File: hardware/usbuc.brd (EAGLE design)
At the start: 24.1 x 20.3 mm, 15 parts, among them J1 PROGRAM, J2 DEVICE, U1 NCP551, U2 AT25SF081-XMHD-T, U3 PIC32MX250F128B-I_ML, Y1 8MHz

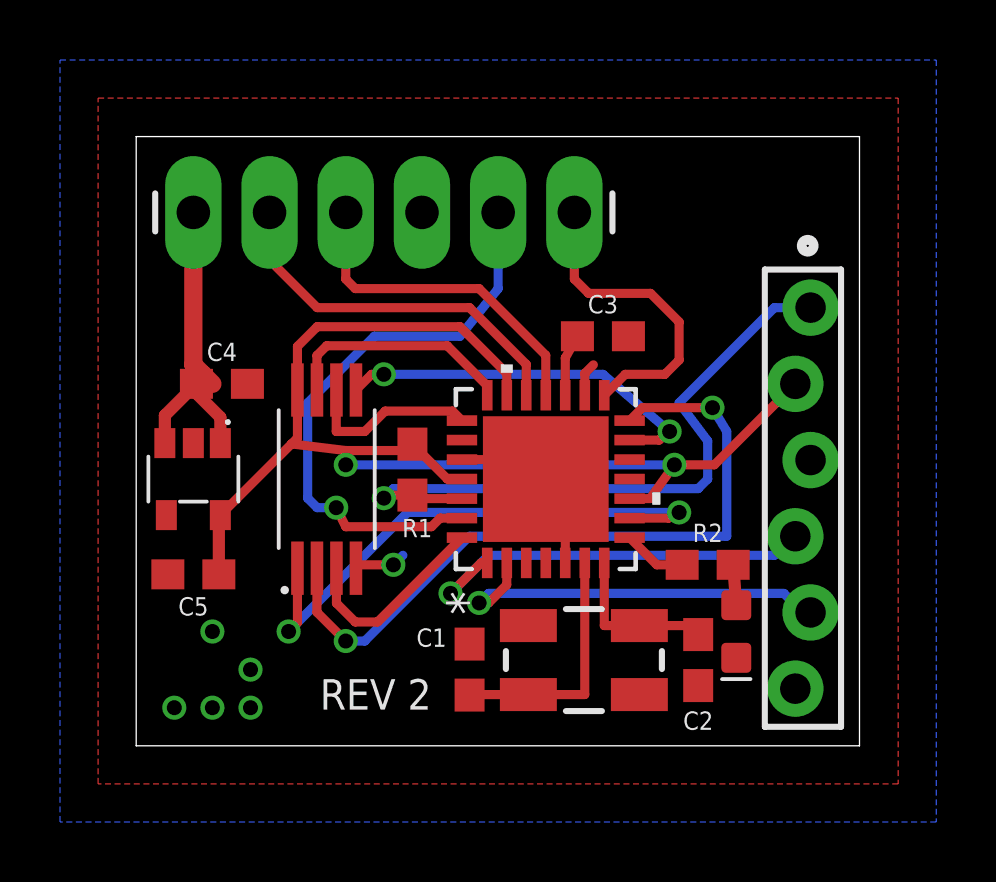
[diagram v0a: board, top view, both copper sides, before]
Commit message: Clear up crystal values in schematic
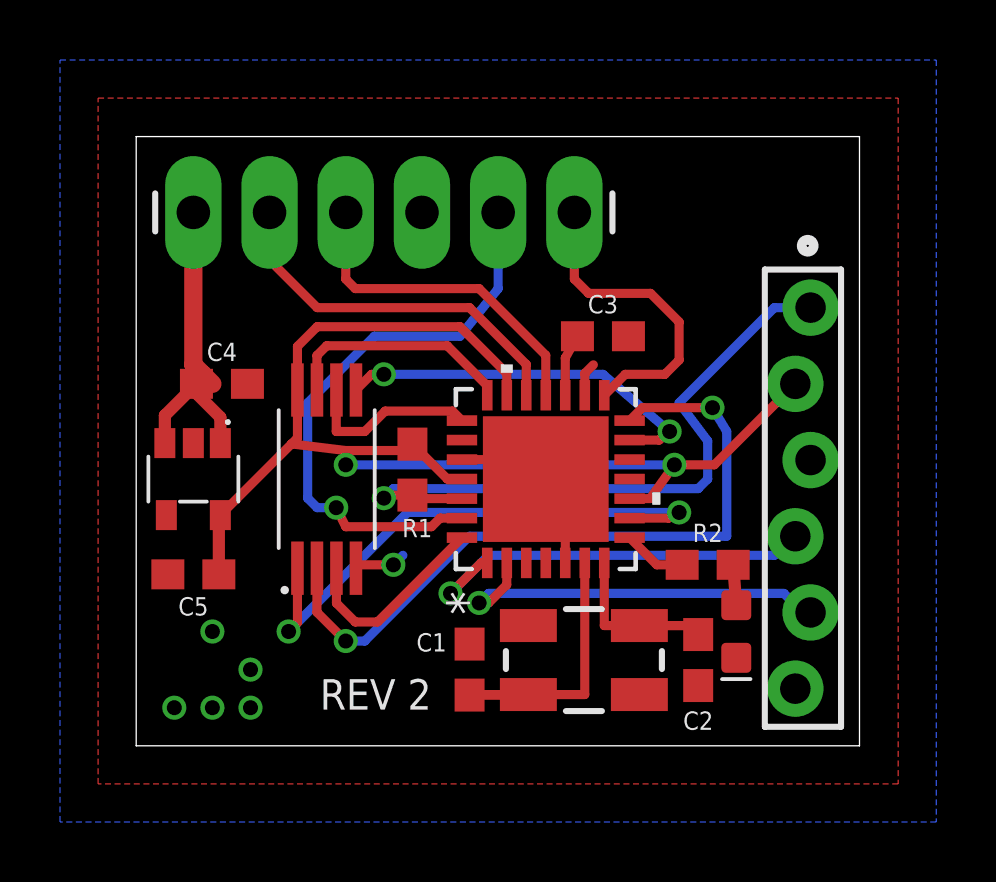
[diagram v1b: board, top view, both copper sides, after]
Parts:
- C1, C2: value 10pF -> 18pF
- moved FRAME1 4.58 mm to (0.00, 0.00)
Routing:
- net N$6: track 5.34 -> 7.81 mm
- net N$5: track 8.23 -> 10.2 mm
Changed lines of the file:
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@@
 <attribute name="PROD_ID" value="XTAL-09431" x="14.9225" y="2.8575" size="1.778" layer="27" rot="R180" display="off"/>
-</element>
-<element name="C1" library="SparkFun-Capacitors" package="0603" value="10pF" x="11.1125" y="2.54" smashed="yes" rot="R270">
-<attribute name="PROD_ID" value="CAP-11812" x="11.1125" y="2.54" size="1.778" layer="27" rot="R270" display="off"/>
-<attribute name="NAME" x="9.8425" y="3.302" size="0.6096" layer="25" font="vector" ratio="20" align="bottom-center"/>
-</element>
-<element name="C2" library="SparkFun-Capacitors" package="0603" value="10pF" x="18.7325" y="2.8575" smashed="yes" rot="R90">
-<attribute name="PROD_ID" value="CAP-11812" x="18.7325" y="2.8575" size="1.778" layer="27" rot="R90" display="off"/>
-<attribute name="NAME" x="18.7325" y="1.143" size="0.6096" layer="25" font="vector" ratio="20" rot="R180" align="bottom-center"/>
 </element>
 <element name="C3" library="SparkFun-Capacitors" package="0603" value="10uF" x="15.5575" y="13.6525" smashed="yes">
@@
 <attribute name="NAME" x="2.8575" y="12.827" size="0.6096" layer="25" font="vector" ratio="20" align="bottom-center"/>
 </element>
-<element name="FRAME1" library="SparkFun-Aesthetics" package="DUMMY" value="FRAME-A4L" x="-2.54" y="-3.81">
-<attribute name="VERSION" value="v01" x="-2.54" y="-3.81" size="1.778" layer="27" display="off"/>
-<attribute name="DESIGNER" value="Nobody" x="-2.54" y="-3.81" size="1.778" layer="27" display="off"/>
+<element name="FRAME1" library="SparkFun-Aesthetics" package="DUMMY" value="FRAME-A4L" x="0" y="0">
+<attribute name="VERSION" value="v01" x="0" y="0" size="1.778" layer="27" display="off"/>
+<attribute name="DESIGNER" value="Nobody" x="0" y="0" size="1.778" layer="27" display="off"/>
+</element>
+<element name="C1" library="SparkFun-Capacitors" package="0603" value="18pF" x="11.1125" y="2.54" smashed="yes" rot="R270">
+<attribute name="PROD_ID" value="CAP-08267" x="11.1125" y="2.54" size="1.778" layer="27" rot="R270" display="off"/>
+<attribute name="NAME" x="9.8425" y="3.14325" size="0.6096" layer="25" font="vector" ratio="20" align="bottom-center"/>
+</element>
+<element name="C2" library="SparkFun-Capacitors" package="0603" value="18pF" x="18.7325" y="2.8575" smashed="yes" rot="R90">
+<attribute name="PROD_ID" value="CAP-08267" x="18.7325" y="2.8575" size="1.778" layer="27" rot="R90" display="off"/>
+<attribute name="NAME" x="18.7325" y="1.143" size="0.6096" layer="25" font="vector" ratio="20" rot="R180" align="bottom-center"/>
 </element>
 </elements>
@@
 <signal name="N$5">
 <contactref element="Y1" pad="3"/>
-<contactref element="C1" pad="2"/>
 <contactref element="U3" pad="6"/>
 <wire x1="13.0725" y1="1.7075" x2="14.9525" y2="1.7075" width="0.3048" layer="1"/>
@@
 <wire x1="13.0725" y1="1.7075" x2="11.43" y2="1.7075" width="0.3048" layer="1"/>
 <wire x1="11.43" y1="1.7075" x2="11.1125" y2="1.69" width="0.3048" layer="1"/>
+<contactref element="C1" pad="2"/>
+<wire x1="11.1125" y1="1.69" x2="13.0175" y2="1.69" width="0.3048" layer="1"/>
+<wire x1="13.0175" y1="1.69" x2="13.0175" y2="1.74625" width="0.3048" layer="1"/>
 </signal>
 <signal name="N$6">
 <contactref element="Y1" pad="1"/>
-<contactref element="C2" pad="2"/>
 <contactref element="U3" pad="7"/>
 <wire x1="16.7725" y1="4.0075" x2="15.6025" y2="4.0075" width="0.3048" layer="1"/>
@@
 <wire x1="16.7725" y1="4.0075" x2="18.415" y2="4.0075" width="0.3048" layer="1"/>
 <wire x1="18.415" y1="4.0075" x2="18.7325" y2="3.7075" width="0.3048" layer="1"/>
+<contactref element="C2" pad="2"/>
+<wire x1="16.7725" y1="4.0075" x2="19.05" y2="4.0075" width="0.3048" layer="1"/>
+<wire x1="19.05" y1="4.0075" x2="19.05" y2="3.81" width="0.3048" layer="1"/>
 </signal>
 <signal name="GND">
-<contactref element="C1" pad="1"/>
-<contactref element="C2" pad="1"/>
 <polygon width="0.1524" layer="1">
 <vertex x="-1.27" y="21.59"/>
@@
 <contactref element="C5" pad="2"/>
 <contactref element="C4" pad="2"/>
+<contactref element="C1" pad="1"/>
+<contactref element="C2" pad="1"/>
 </signal>
 <signal name="3.3V">
